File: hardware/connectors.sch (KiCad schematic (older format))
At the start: 16 parts

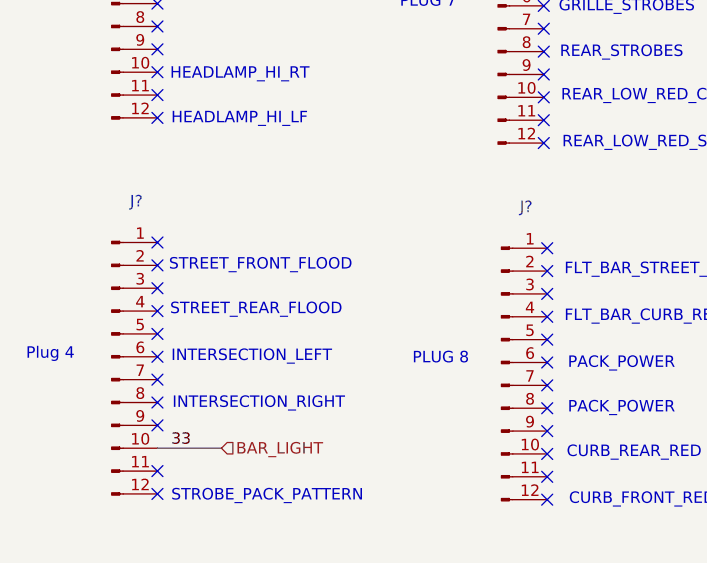
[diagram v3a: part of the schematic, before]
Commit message: hardware: add driver flood wires
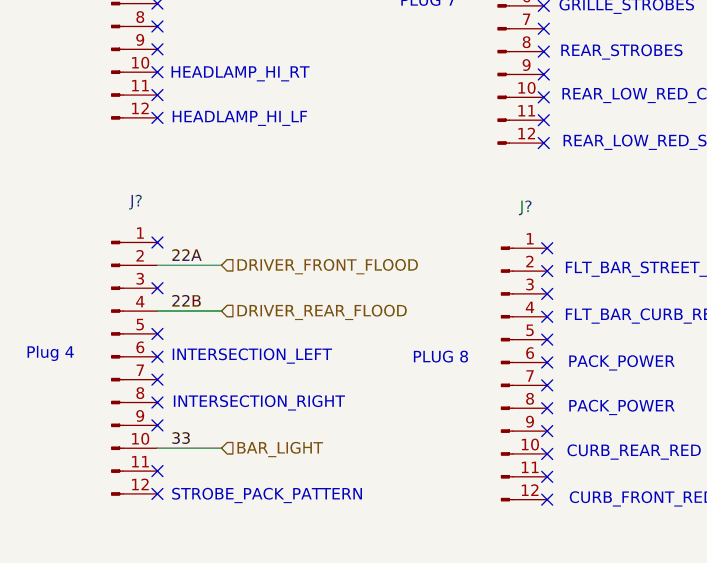
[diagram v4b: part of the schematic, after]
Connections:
- net DRIVER_FRONT_FLOOD: now reaches J?.2 (Pin_2)
- net DRIVER_REAR_FLOOD: now reaches J?.4 (Pin_4)
- no-connect marks 159 -> 157
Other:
- note removed: "STREET_FRONT_FLOOD"
- note removed: "STREET_REAR_FLOOD"
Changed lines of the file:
@@
 NoConn ~ 1245 6435
 NoConn ~ 1245 6335
-NoConn ~ 1245 6235
 NoConn ~ 1245 6135
-NoConn ~ 1245 6035
 NoConn ~ 1245 5935
 Text Notes 1305 7075 0    50   ~ 0
@@
 Text Notes 1305 6465 0    50   ~ 0
 INTERSECTION_LEFT
-Text Notes 1300 6260 0    50   ~ 0
-STREET_REAR_FLOOD
-Text Notes 1295 6065 0    50   ~ 0
-STREET_FRONT_FLOOD
 NoConn ~ 2930 2900
 NoConn ~ 2930 3000
@@
 Text Notes 4630 1385 0    50   ~ 0
 HVAC_BLOWER
+Text Label 1305 6235 0    50   ~ 0
+22B
+Text HLabel 1525 6235 2    50   Input ~ 0
+DRIVER_REAR_FLOOD
+Wire Wire Line
+	1245 6235 1525 6235
+Text Label 1305 6035 0    50   ~ 0
+22A
+Text HLabel 1525 6035 2    50   Input ~ 0
+DRIVER_FRONT_FLOOD
+Wire Wire Line
+	1245 6035 1525 6035
 $EndSCHEMATC

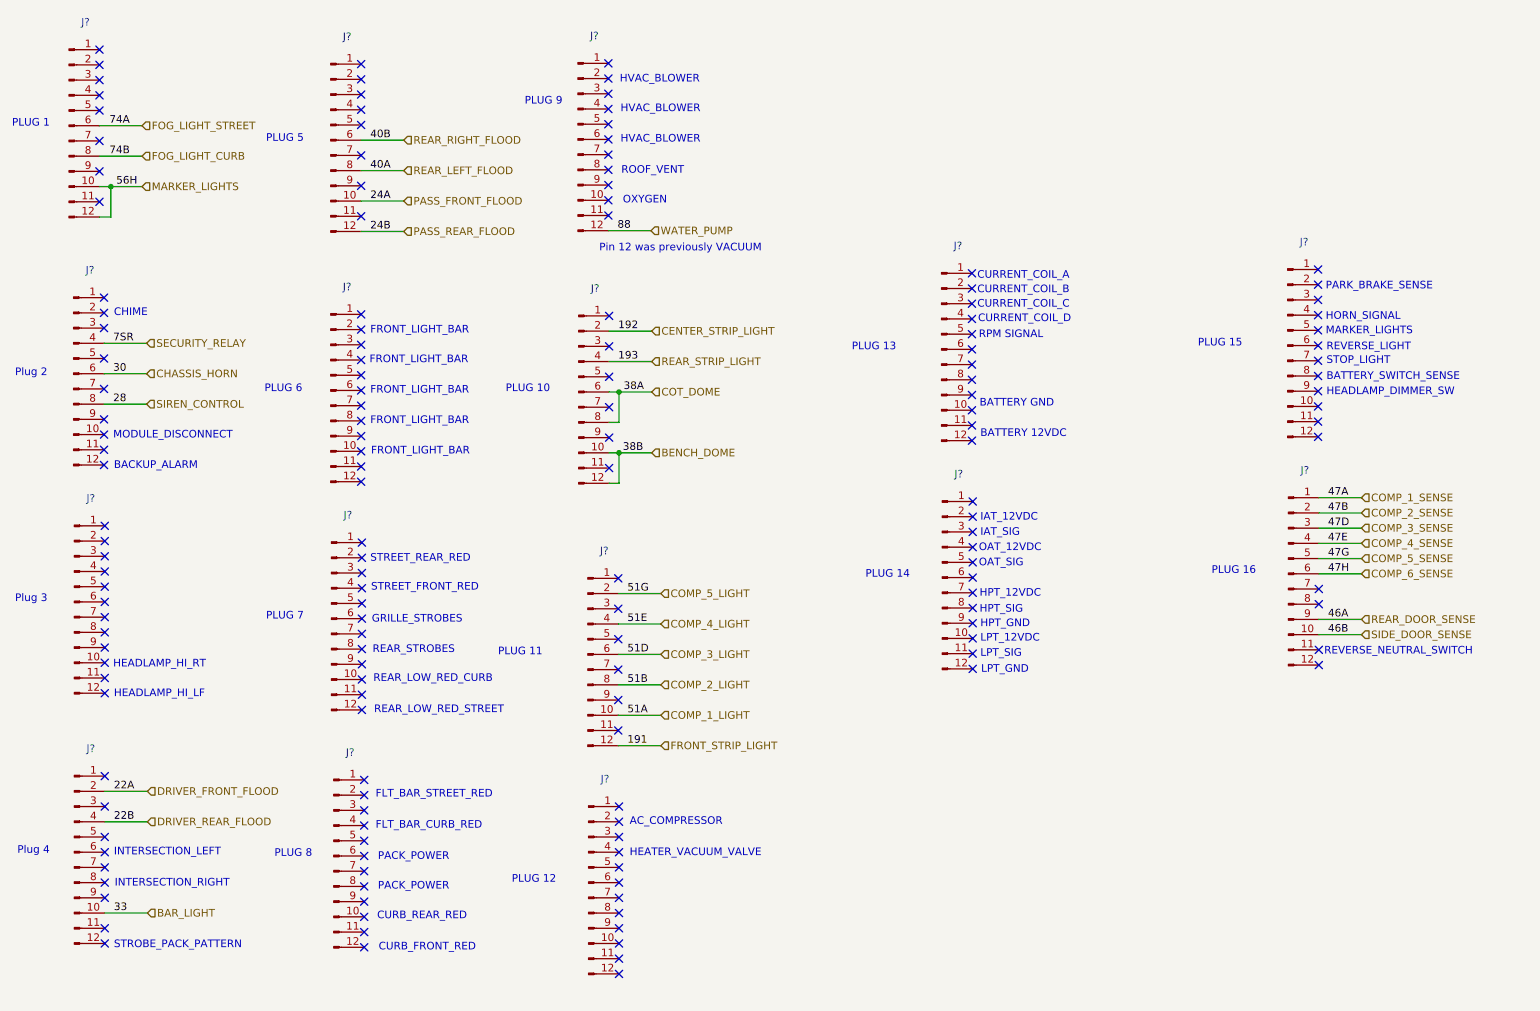
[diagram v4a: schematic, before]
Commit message: hardware: add Horton circuit numbers to unused pins on connectors
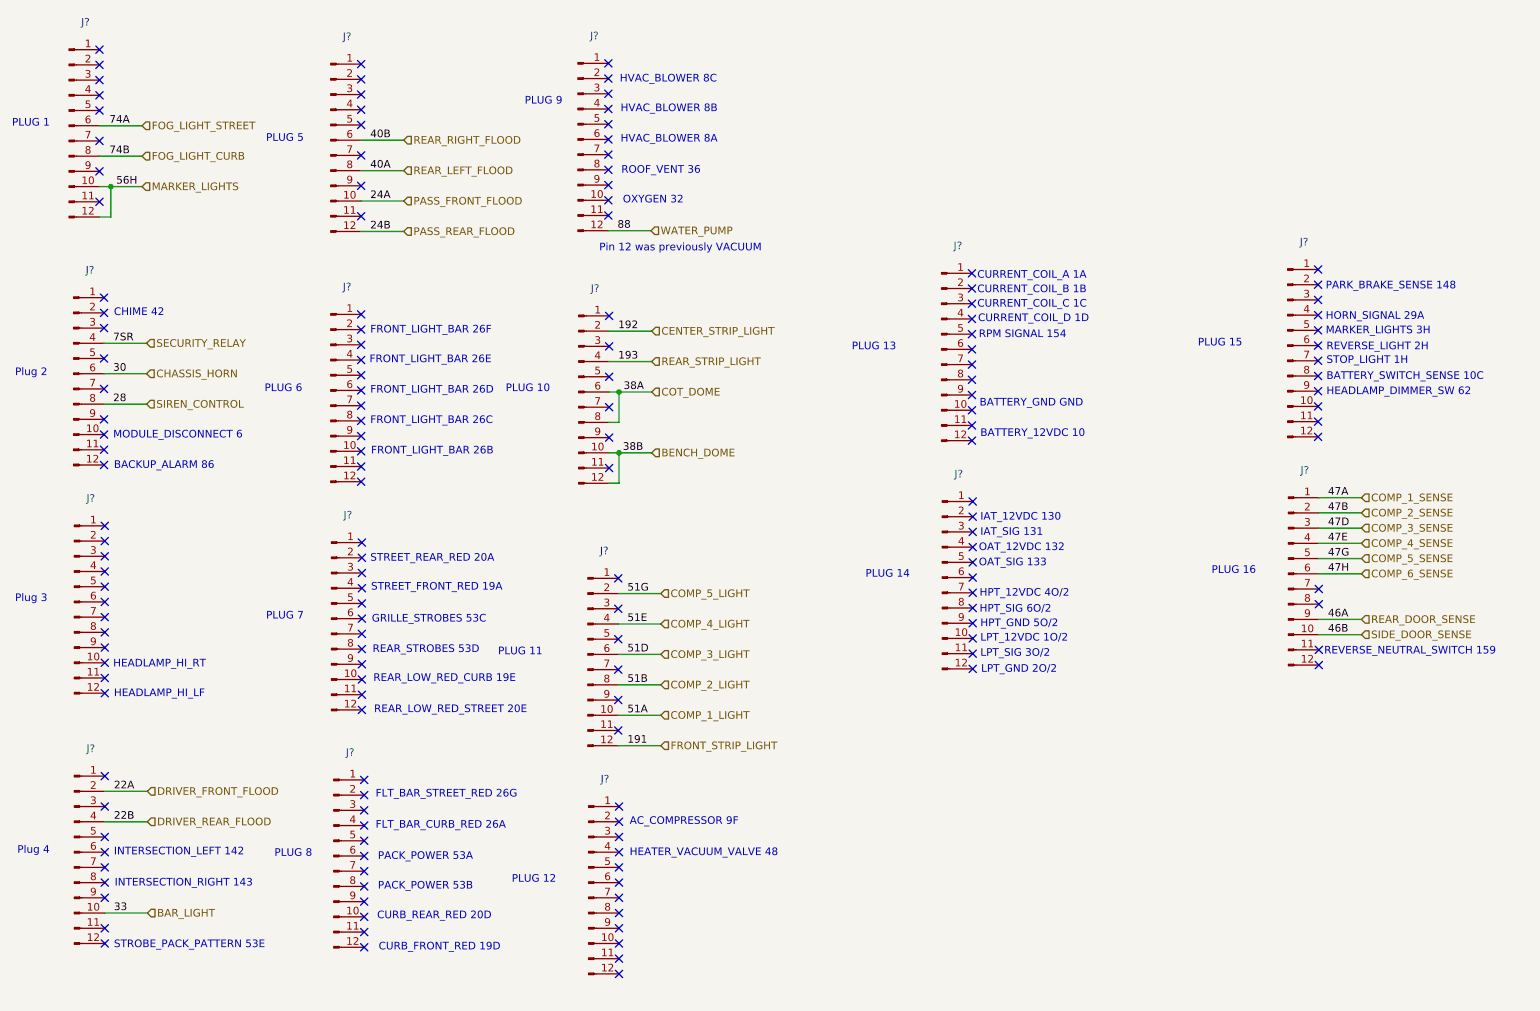
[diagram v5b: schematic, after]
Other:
- note added: "AC_COMPRESSOR 9F"
- note added: "BACKUP_ALARM 86"
- note added: "BATTERY_12VDC 10"
- note added: "BATTERY_GND GND"
- note added: "BATTERY_SWITCH_SENSE 10C"
- note added: "CHIME 42"
- note added: "CURB_FRONT_RED 19D"
- note added: "CURB_REAR_RED 20D"
- note added: "CURRENT_COIL_A 1A"
- note added: "CURRENT_COIL_B 1B"
- note added: "CURRENT_COIL_C 1C"
- note added: "CURRENT_COIL_D 1D"
- note added: "FLT_BAR_CURB_RED 26A"
- note added: "FLT_BAR_STREET_RED 26G"
- note added: "FRONT_LIGHT_BAR 26B"
- note added: "FRONT_LIGHT_BAR 26C"
- note added: "FRONT_LIGHT_BAR 26D"
- note added: "FRONT_LIGHT_BAR 26E"
- note added: "FRONT_LIGHT_BAR 26F"
- note added: "GRILLE_STROBES 53C"
- note added: "HEADLAMP_DIMMER_SW 62"
- note added: "HEATER_VACUUM_VALVE 48"
- note added: "HORN_SIGNAL 29A"
- note added: "HPT_12VDC 4O/2"
- note added: "HPT_GND 5O/2"
- note added: "HPT_SIG 6O/2"
- note added: "HVAC_BLOWER 8A"
- note added: "HVAC_BLOWER 8B"
- note added: "HVAC_BLOWER 8C"
- note added: "IAT_12VDC 130"
- note added: "IAT_SIG 131"
- note added: "INTERSECTION_LEFT 142"
- note added: "INTERSECTION_RIGHT 143"
- note added: "LPT_12VDC 1O/2"
- note added: "LPT_GND 2O/2"
- note added: "LPT_SIG 3O/2"
- note added: "MARKER_LIGHTS 3H"
- note added: "MODULE_DISCONNECT 6"
- note added: "OAT_12VDC 132"
- note added: "OAT_SIG 133"
- note added: "OXYGEN 32"
- note added: "PACK_POWER 53A"
- note added: "PACK_POWER 53B"
- note added: "PARK_BRAKE_SENSE 148"
- note added: "REAR_LOW_RED_CURB 19E"
- note added: "REAR_LOW_RED_STREET 20E"
- note added: "REAR_STROBES 53D"
- note added: "REVERSE_LIGHT 2H"
- note added: "REVERSE_NEUTRAL_SWITCH 159"
- note added: "ROOF_VENT 36"
- note added: "RPM SIGNAL 154"
- note added: "STOP_LIGHT 1H"
- note added: "STREET_FRONT_RED 19A"
- note added: "STREET_REAR_RED 20A"
- note added: "STROBE_PACK_PATTERN 53E"
- note removed: "AC_COMPRESSOR"
- note removed: "BACKUP_ALARM"
- note removed: "BATTERY 12VDC"
- note removed: "BATTERY GND"
- note removed: "BATTERY_SWITCH_SENSE"
- note removed: "CHIME"
- note removed: "CURB_FRONT_RED"
- note removed: "CURB_REAR_RED"
- note removed: "CURRENT_COIL_A"
- note removed: "CURRENT_COIL_B"
- note removed: "CURRENT_COIL_C"
- note removed: "CURRENT_COIL_D"
- note removed: "FLT_BAR_CURB_RED"
- note removed: "FLT_BAR_STREET_RED"
- note removed: "FRONT_LIGHT_BAR"
- note removed: "GRILLE_STROBES"
- note removed: "HEADLAMP_DIMMER_SW"
- note removed: "HEATER_VACUUM_VALVE"
- note removed: "HORN_SIGNAL"
- note removed: "HPT_12VDC"
- note removed: "HPT_GND"
- note removed: "HPT_SIG"
- note removed: "HVAC_BLOWER"
- note removed: "IAT_12VDC"
- note removed: "IAT_SIG"
- note removed: "INTERSECTION_LEFT"
- note removed: "INTERSECTION_RIGHT"
- note removed: "LPT_12VDC"
- note removed: "LPT_GND"
- note removed: "LPT_SIG"
- note removed: "MARKER_LIGHTS"
- note removed: "MODULE_DISCONNECT"
- note removed: "OAT_12VDC"
- note removed: "OAT_SIG"
- note removed: "OXYGEN"
- note removed: "PACK_POWER"
- note removed: "PARK_BRAKE_SENSE"
- note removed: "REAR_LOW_RED_CURB"
- note removed: "REAR_LOW_RED_STREET"
- note removed: "REAR_STROBES"
- note removed: "REVERSE_LIGHT"
- note removed: "REVERSE_NEUTRAL_SWITCH"
- note removed: "ROOF_VENT"
- note removed: "RPM SIGNAL"
- note removed: "STOP_LIGHT"
- note removed: "STREET_FRONT_RED"
- note removed: "STREET_REAR_RED"
- note removed: "STROBE_PACK_PATTERN"
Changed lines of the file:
@@
 NoConn ~ 9225 5205
 Text Notes 9260 5145 0    50   ~ 0
-REVERSE_NEUTRAL_SWITCH
+REVERSE_NEUTRAL_SWITCH 159
 Text Notes 4695 6265 0    50   ~ 0
-AC_COMPRESSOR
+AC_COMPRESSOR 9F
 Text Notes 4695 6470 0    50   ~ 0
-HEATER_VACUUM_VALVE
+HEATER_VACUUM_VALVE 48
 NoConn ~ 4625 6135
 NoConn ~ 4625 6235
@@
 NoConn ~ 4625 7235
 Text Notes 7000 3715 0    50   ~ 0
-BATTERY 12VDC
+BATTERY_12VDC 10
 Text Notes 6995 3515 0    50   ~ 0
-BATTERY GND
+BATTERY_GND GND
 Text Notes 6990 3065 0    50   ~ 0
-RPM SIGNAL
+RPM SIGNAL 154
 Text Notes 6985 2960 0    50   ~ 0
-CURRENT_COIL_D
+CURRENT_COIL_D 1D
 Text Notes 6980 2865 0    50   ~ 0
-CURRENT_COIL_C
+CURRENT_COIL_C 1C
 Text Notes 6980 2770 0    50   ~ 0
-CURRENT_COIL_B
+CURRENT_COIL_B 1B
 Text Notes 6980 2675 0    50   ~ 0
-CURRENT_COIL_A
+CURRENT_COIL_A 1A
 NoConn ~ 6945 2630
 NoConn ~ 6945 2730
@@
 NoConn ~ 6950 4130
 Text Notes 7005 5265 0    50   ~ 0
-LPT_GND
+LPT_GND 2O/2
 Text Notes 7000 5160 0    50   ~ 0
-LPT_SIG
+LPT_SIG 3O/2
 Text Notes 7000 5060 0    50   ~ 0
-LPT_12VDC
+LPT_12VDC 1O/2
 Text Notes 7000 4965 0    50   ~ 0
-HPT_GND
+HPT_GND 5O/2
 Text Notes 6995 4870 0    50   ~ 0
-HPT_SIG
+HPT_SIG 6O/2
 Text Notes 6995 4765 0    50   ~ 0
-HPT_12VDC
+HPT_12VDC 4O/2
 Text Notes 6990 4565 0    50   ~ 0
-OAT_SIG
+OAT_SIG 133
 Text Notes 6990 4465 0    50   ~ 0
-OAT_12VDC
+OAT_12VDC 132
 Text Notes 7000 4365 0    50   ~ 0
-IAT_SIG
+IAT_SIG 131
 Text Notes 7000 4265 0    50   ~ 0
-IAT_12VDC
+IAT_12VDC 130
 NoConn ~ 9220 2605
 NoConn ~ 9220 2705
@@
 NoConn ~ 9220 3705
 Text Notes 9275 3440 0    50   ~ 0
-HEADLAMP_DIMMER_SW
+HEADLAMP_DIMMER_SW 62
 Text Notes 9275 3340 0    50   ~ 0
-BATTERY_SWITCH_SENSE
+BATTERY_SWITCH_SENSE 10C
 Text Notes 9275 3235 0    50   ~ 0
-STOP_LIGHT
+STOP_LIGHT 1H
 Text Notes 9275 3145 0    50   ~ 0
-REVERSE_LIGHT
+REVERSE_LIGHT 2H
 Text Notes 9270 3040 0    50   ~ 0
-MARKER_LIGHTS
+MARKER_LIGHTS 3H
 Text Notes 9270 2945 0    50   ~ 0
-HORN_SIGNAL
+HORN_SIGNAL 29A
 Text Notes 9270 2745 0    50   ~ 0
-PARK_BRAKE_SENSE
+PARK_BRAKE_SENSE 148
 Text Notes 1305 3925 0    50   ~ 0
-BACKUP_ALARM
+BACKUP_ALARM 86
 Text Notes 1300 3725 0    50   ~ 0
-MODULE_DISCONNECT
+MODULE_DISCONNECT 6
 Text Notes 1305 2920 0    50   ~ 0
-CHIME
+CHIME 42
 Text Notes 1305 5425 0    50   ~ 0
 HEADLAMP_HI_LF
@@
 NoConn ~ 1245 5935
 Text Notes 1305 7075 0    50   ~ 0
-STROBE_PACK_PATTERN
+STROBE_PACK_PATTERN 53E
 Text Notes 1310 6670 0    50   ~ 0
-INTERSECTION_RIGHT
+INTERSECTION_RIGHT 143
 Text Notes 1305 6465 0    50   ~ 0
-INTERSECTION_LEFT
+INTERSECTION_LEFT 142
 NoConn ~ 2930 2900
 NoConn ~ 2930 3000
@@
 NoConn ~ 2950 7060
 Text Notes 2995 3830 0    50   ~ 0
-FRONT_LIGHT_BAR
+FRONT_LIGHT_BAR 26B
 Text Notes 2990 3630 0    50   ~ 0
-FRONT_LIGHT_BAR
+FRONT_LIGHT_BAR 26C
 Text Notes 2990 3430 0    50   ~ 0
-FRONT_LIGHT_BAR
+FRONT_LIGHT_BAR 26D
 Text Notes 2985 3230 0    50   ~ 0
-FRONT_LIGHT_BAR
+FRONT_LIGHT_BAR 26E
 Text Notes 2990 3035 0    50   ~ 0
-FRONT_LIGHT_BAR
+FRONT_LIGHT_BAR 26F
 Text Notes 3015 5530 0    50   ~ 0
-REAR_LOW_RED_STREET
+REAR_LOW_RED_STREET 20E
 Text Notes 3010 5325 0    50   ~ 0
-REAR_LOW_RED_CURB
+REAR_LOW_RED_CURB 19E
 Text Notes 3005 5135 0    50   ~ 0
-REAR_STROBES
+REAR_STROBES 53D
 Text Notes 3000 4935 0    50   ~ 0
-GRILLE_STROBES
+GRILLE_STROBES 53C
 Text Notes 2995 4725 0    50   ~ 0
-STREET_FRONT_RED
+STREET_FRONT_RED 19A
 Text Notes 2990 4535 0    50   ~ 0
-STREET_REAR_RED
+STREET_REAR_RED 20A
 Text Notes 3045 7090 0    50   ~ 0
-CURB_FRONT_RED
+CURB_FRONT_RED 19D
 Text Notes 3035 6885 0    50   ~ 0
-CURB_REAR_RED
+CURB_REAR_RED 20D
 Text Notes 3040 6690 0    50   ~ 0
-PACK_POWER
+PACK_POWER 53B
 Text Notes 3040 6495 0    50   ~ 0
-PACK_POWER
+PACK_POWER 53A
 Text Notes 3025 6290 0    50   ~ 0
-FLT_BAR_CURB_RED
+FLT_BAR_CURB_RED 26A
 Text Notes 3025 6085 0    50   ~ 0
-FLT_BAR_STREET_RED
+FLT_BAR_STREET_RED 26G
 NoConn ~ 4555 2250
 NoConn ~ 4555 2150
@@
 Pin 12 was previously VACUUM
 Text Notes 4650 2180 0    50   ~ 0
-OXYGEN
+OXYGEN 32
 Text Notes 4640 1985 0    50   ~ 0
-ROOF_VENT
+ROOF_VENT 36
 Text Notes 4635 1780 0    50   ~ 0
-HVAC_BLOWER
+HVAC_BLOWER 8A
 Text Notes 4635 1580 0    50   ~ 0
-HVAC_BLOWER
+HVAC_BLOWER 8B
 Text Notes 4630 1385 0    50   ~ 0
-HVAC_BLOWER
+HVAC_BLOWER 8C
 Text Label 1305 6235 0    50   ~ 0
 22B
